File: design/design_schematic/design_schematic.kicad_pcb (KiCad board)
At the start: 2 copper layers, 22 parts, among them U1 nRF52840, X1 32MHz

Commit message: pcb place switches, leds, diodes and stabiliser right side
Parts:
- added C10: 4.7uF, ScottoKeebs_Components:Capacitor_0402, F.Cu at (553.7, 104.6)
- added C13: 4.7uF, ScottoKeebs_Components:Capacitor_0402, F.Cu at (553.7, 110.5)
- added C17: 4.7uF, ScottoKeebs_Components:Capacitor_0402, F.Cu at (553.7, 114.5)
- added C18: 1uF, ScottoKeebs_Components:Capacitor_0402, F.Cu at (553.7, 116.5)
- added C22: 470nF, ScottoKeebs_Components:Capacitor_0402, F.Cu at (553.7, 118.4)
- added C23: 4.7uF, ScottoKeebs_Components:Capacitor_0402, F.Cu at (556.5, 104.6)
- added C24: 100nF, ScottoKeebs_Components:Capacitor_0402, F.Cu at (556.5, 106.6)
- added C25: 10uF, ScottoKeebs_Components:Capacitor_0402, F.Cu at (556.5, 108.6)
- added C26: 10uF, ScottoKeebs_Components:Capacitor_0402, F.Cu at (556.5, 110.5)
- added C27: 10uF, ScottoKeebs_Components:Capacitor_0402, F.Cu at (556.5, 112.5)
- added C28: 100nF, ScottoKeebs_Components:Capacitor_0402, F.Cu at (556.5, 114.5)
- added C31: 100nF, ScottoKeebs_Components:Capacitor_0402, F.Cu at (556.5, 116.5)
- added C34: 100nF, ScottoKeebs_Components:Capacitor_0402, F.Cu at (556.5, 118.4)
- added C37: 100nF, ScottoKeebs_Components:Capacitor_0402, F.Cu at (559.4, 104.6)
- added C40: 100nF, ScottoKeebs_Components:Capacitor_0402, F.Cu at (559.4, 106.6)
- added C43: 100nF, ScottoKeebs_Components:Capacitor_0402, F.Cu at (559.4, 108.6)
- added C46: 10uF, ScottoKeebs_Components:Capacitor_0402, F.Cu at (559.4, 110.5)
- added C49: 100nF, ScottoKeebs_Components:Capacitor_0402, F.Cu at (559.4, 112.5)
- added C9: 4.7uF, ScottoKeebs_Components:Capacitor_0402, F.Cu at (550.8, 118.4)
- added D1: LED_SK6812MINI, ScottoKeebs_Components:LED_SK6812MINI, B.Cu at (74.4, 47.2)
- added D10: LED_SK6812MINI, ScottoKeebs_Components:LED_SK6812MINI, B.Cu at (131.5, 66.2)
- added D11: LED_SK6812MINI, ScottoKeebs_Components:LED_SK6812MINI, B.Cu at (150.6, 66.2)
- added D12: LED_SK6812MINI, ScottoKeebs_Components:LED_SK6812MINI, B.Cu at (169.6, 66.2)
- added D13: LED_SK6812MINI, ScottoKeebs_Components:LED_SK6812MINI, B.Cu at (74.4, 85.3)
- added D14: LED_SK6812MINI, ScottoKeebs_Components:LED_SK6812MINI, B.Cu at (93.4, 85.3)
- added D15: LED_SK6812MINI, ScottoKeebs_Components:LED_SK6812MINI, B.Cu at (112.5, 85.3)
- added D16: LED_SK6812MINI, ScottoKeebs_Components:LED_SK6812MINI, B.Cu at (131.5, 85.3)
- added D17: LED_SK6812MINI, ScottoKeebs_Components:LED_SK6812MINI, B.Cu at (150.6, 85.3)
- added D18: LED_SK6812MINI, ScottoKeebs_Components:LED_SK6812MINI, B.Cu at (172.0, 85.3)
- added D19: LED_SK6812MINI, ScottoKeebs_Components:LED_SK6812MINI, B.Cu at (88.7, 104.3)
- added D2: LED_SK6812MINI, ScottoKeebs_Components:LED_SK6812MINI, B.Cu at (93.4, 47.2)
- added D20: LED_SK6812MINI, ScottoKeebs_Components:LED_SK6812MINI, B.Cu at (117.3, 104.3)
- added D21: LED_SK6812MINI, ScottoKeebs_Components:LED_SK6812MINI, B.Cu at (136.3, 104.3)
- added D22: LED_SK6812MINI, ScottoKeebs_Components:LED_SK6812MINI, B.Cu at (155.4, 104.3)
- added D23: LED_SK6812MINI, ScottoKeebs_Components:LED_SK6812MINI, B.Cu at (174.4, 104.3)
- added D24: LED_SK6812MINI, ScottoKeebs_Components:LED_SK6812MINI, B.Cu at (69.6, 123.4)
- added D3: LED_SK6812MINI, ScottoKeebs_Components:LED_SK6812MINI, B.Cu at (112.5, 47.2)
- added D4: LED_SK6812MINI, ScottoKeebs_Components:LED_SK6812MINI, B.Cu at (131.5, 47.2)
- added D5: LED_SK6812MINI, ScottoKeebs_Components:LED_SK6812MINI, B.Cu at (150.6, 47.2)
- added D6: LED_SK6812MINI, ScottoKeebs_Components:LED_SK6812MINI, B.Cu at (172.0, 47.2)
- added D7: LED_SK6812MINI, ScottoKeebs_Components:LED_SK6812MINI, B.Cu at (74.4, 66.2)
- added D8: LED_SK6812MINI, ScottoKeebs_Components:LED_SK6812MINI, B.Cu at (93.4, 66.2)
- added D9: LED_SK6812MINI, ScottoKeebs_Components:LED_SK6812MINI, B.Cu at (112.5, 66.2)
- added Di1: Diode, ScottoKeebs_Components:Diode_SOD-123, B.Cu at (82.9, 45.5)
- added Di10: Diode, ScottoKeebs_Components:Diode_SOD-123, B.Cu at (180.5, 45.5)
- added Di11: Diode, ScottoKeebs_Components:Diode_SOD-123, B.Cu at (82.9, 64.5)
- added Di12: Diode, ScottoKeebs_Components:Diode_SOD-123, B.Cu at (101.9, 64.5)
- added Di13: Diode, ScottoKeebs_Components:Diode_SOD-123, B.Cu at (140.0, 64.5)
- added Di14: Diode, ScottoKeebs_Components:Diode_SOD-123, B.Cu at (159.1, 64.5)
- added Di15: Diode, ScottoKeebs_Components:Diode_SOD-123, B.Cu at (178.1, 64.5)
- added Di16: Diode, ScottoKeebs_Components:Diode_SOD-123, B.Cu at (101.9, 83.6)
- added Di17: Diode, ScottoKeebs_Components:Diode_SOD-123, B.Cu at (121.0, 83.6)
- added Di18: Diode, ScottoKeebs_Components:Diode_SOD-123, B.Cu at (140.0, 83.6)
- added Di19: Diode, ScottoKeebs_Components:Diode_SOD-123, B.Cu at (88.7, 104.3)
- added Di2: Diode, ScottoKeebs_Components:Diode_SOD-123, B.Cu at (159.1, 45.5)
- added Di20: Diode, ScottoKeebs_Components:Diode_SOD-123, B.Cu at (97.2, 102.6)
- added Di21: Diode, ScottoKeebs_Components:Diode_SOD-123, B.Cu at (125.8, 102.6)
- added Di22: Diode, ScottoKeebs_Components:Diode_SOD-123, B.Cu at (163.9, 102.6)
- added Di23: Diode, ScottoKeebs_Components:Diode_SOD-123, B.Cu at (182.9, 102.6)
- added Di24: Diode, ScottoKeebs_Components:Diode_SOD-123, B.Cu at (78.1, 121.7)
- added Di3: Diode, ScottoKeebs_Components:Diode_SOD-123, B.Cu at (121.0, 64.5)
- added Di4: Diode, ScottoKeebs_Components:Diode_SOD-123, B.Cu at (82.9, 83.6)
- added Di5: Diode, ScottoKeebs_Components:Diode_SOD-123, B.Cu at (159.1, 83.6)
- added Di6: Diode, ScottoKeebs_Components:Diode_SOD-123, B.Cu at (144.8, 102.6)
- added Di7: Diode, ScottoKeebs_Components:Diode_SOD-123, B.Cu at (101.9, 45.5)
- added Di8: Diode, ScottoKeebs_Components:Diode_SOD-123, B.Cu at (121.0, 45.5)
- added Di9: Diode, ScottoKeebs_Components:Diode_SOD-123, B.Cu at (140.0, 45.5)
- added IC1: XC9291B33D0R-G, SamacSys_Parts:XC9290A07E0RG, F.Cu at (546.8, 146.9)
- added IC4: 74AHCT125PW,118, SamacSys_Parts:SOP65P640X110-14N, F.Cu at (540.9, 142.1)
- added J1: USB_C_Receptacle_USB2.0_16P, Connector_USB:USB_C_Receptacle_HRO_TYPE-C-31-M-12, F.Cu at (539.9, 129.5)
- added J4: OLED_128x32, ScottoKeebs_Components:OLED_128x32, F.Cu at (531.1, 124.5)
- added J5: 0781271220, SamacSys_Parts:0781271220, F.Cu at (551.4, 125.7)
- added S1: Keyswitch, ScottoKeebs_Hotswap:Hotswap_Choc_V1_1.00u, F.Cu at (74.4, 42.5)
- added S10: Keyswitch, ScottoKeebs_Hotswap:Hotswap_Choc_V1_1.00u, F.Cu at (131.5, 61.5)
- added S11: Keyswitch, ScottoKeebs_Hotswap:Hotswap_Choc_V1_1.00u, F.Cu at (150.6, 61.5)
- added S12: Keyswitch, ScottoKeebs_Hotswap:Hotswap_Choc_V1_1.00u, F.Cu at (172.0, 61.5)
- added S13: Keyswitch, ScottoKeebs_Hotswap:Hotswap_Choc_V1_1.00u, F.Cu at (74.4, 80.6)
- added S14: Keyswitch, ScottoKeebs_Hotswap:Hotswap_Choc_V1_1.00u, F.Cu at (93.4, 80.6)
- added S15: Keyswitch, ScottoKeebs_Hotswap:Hotswap_Choc_V1_1.00u, F.Cu at (112.5, 80.6)
- added S16: Keyswitch, ScottoKeebs_Hotswap:Hotswap_Choc_V1_1.00u, F.Cu at (131.5, 80.6)
- added S17: Keyswitch, ScottoKeebs_Hotswap:Hotswap_Choc_V1_1.00u, F.Cu at (150.6, 80.6)
- added S18: Keyswitch, ScottoKeebs_Hotswap:Hotswap_Choc_V1_1.00u, F.Cu at (172.0, 80.6)
- added S2: Keyswitch, ScottoKeebs_Hotswap:Hotswap_Choc_V1_1.00u, F.Cu at (93.4, 42.5)
- added S20: Keyswitch, ScottoKeebs_Hotswap:Hotswap_Choc_V1_1.00u, F.Cu at (117.3, 99.6)
- added S21: Keyswitch, ScottoKeebs_Hotswap:Hotswap_Choc_V1_1.00u, F.Cu at (136.3, 99.6)
- added S22: Keyswitch, ScottoKeebs_Hotswap:Hotswap_Choc_V1_1.00u, F.Cu at (155.4, 99.6)
- added S23: Keyswitch, ScottoKeebs_Hotswap:Hotswap_Choc_V1_1.00u, F.Cu at (174.4, 99.6)
- added S24: Keyswitch, ScottoKeebs_Hotswap:Hotswap_Choc_V1_1.00u, F.Cu at (69.6, 118.7)
- added S3: Keyswitch, ScottoKeebs_Hotswap:Hotswap_Choc_V1_1.00u, F.Cu at (112.5, 42.5)
- added S4: Keyswitch, ScottoKeebs_Hotswap:Hotswap_Choc_V1_1.00u, F.Cu at (131.5, 42.5)
- added S5: Keyswitch, ScottoKeebs_Hotswap:Hotswap_Choc_V1_1.00u, F.Cu at (150.6, 42.5)
- added S6: Keyswitch, ScottoKeebs_Hotswap:Hotswap_Choc_V1_1.00u, F.Cu at (172.0, 42.5)
- added S7: Keyswitch, ScottoKeebs_Hotswap:Hotswap_Choc_V1_1.00u, F.Cu at (74.4, 61.5)
- added S8: Keyswitch, ScottoKeebs_Hotswap:Hotswap_Choc_V1_1.00u, F.Cu at (93.4, 61.5)
- added S9: Keyswitch, ScottoKeebs_Hotswap:Hotswap_Choc_V1_1.00u, F.Cu at (112.5, 61.5)
- added Si19: Keyswitch, ScottoKeebs_Hotswap:Hotswap_Choc_V1_1.00u, F.Cu at (88.7, 99.6)
- added St1: Stabilizer_MX_2.00u, ScottoKeebs_Stabilizer:Stabilizer_MX_2.00u, F.Cu at (69.6, 118.7)
- added St2: Stabilizer_MX_2.00u, ScottoKeebs_Stabilizer:Stabilizer_MX_2.00u, F.Cu at (88.7, 99.6)
- added U2: BQ24072RGT, Package_DFN_QFN:VQFN-16-1EP_3x3mm_P0.5mm_EP1.6x1.6mm, F.Cu at (556.4, 146.2)
- added U3: USB6B1, Package_SO:SOIC-8_3.9x4.9mm_P1.27mm, F.Cu at (549.5, 142.2)
- added U4: BQ27441-G1, Package_SON:Texas_S-PDSO-N12, F.Cu at (556.9, 141.2)
- added U5: PEC11L-4015F-S0015, SamacSys_Parts:PEC11L4015FS0015, F.Cu at (533.0, 62.1)
- added U6: PEC11L-4015F-S0015, SamacSys_Parts:PEC11L4015FS0015, F.Cu at (551.3, 62.1)
- moved L1 520.5 mm to (560.5, 144.5)
- moved L3 520.5 mm to (560.5, 146.5)
- moved L2 519.6 mm to (561.2, 139.7)
- moved L4 519.6 mm to (561.2, 141.4)
- moved X1 515.2 mm to (551.0, 133.7)
- moved C1 505.7 mm to (550.8, 104.6)
- moved C16 505.7 mm to (553.7, 112.5)
- moved C2 505.7 mm to (550.8, 106.6)
- moved C3 505.7 mm to (550.8, 108.6)
- moved C4 505.7 mm to (550.8, 110.5)
- moved C5 505.7 mm to (550.8, 112.5)
- moved C11 505.4 mm to (553.7, 106.6)
- moved C12 505.4 mm to (553.7, 108.6)
- moved C7 504.6 mm to (550.8, 114.5)
- moved C8 504.6 mm to (550.8, 116.5)
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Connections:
- net VEXT renamed 3V3
- U1 pad A10: unconnected-(U1-AIN5/P0.29-PadA10) -> /NO2
- U1 pad A12: unconnected-(U1-AIN0/P0.02-PadA12) -> /Column 0
- U1 pad A8: unconnected-(U1-AIN7/P0.31-PadA8) -> /NO
- U1 pad AA24: unconnected-(U1-SWDCLK-PadAA24) -> Net-(J6-Pin_4)
- U1 pad AC11: unconnected-(U1-P0.16-PadAC11) -> /SCL
- U1 pad AC13: unconnected-(U1-P0.18/~{RESET}-PadAC13) -> Net-(J6-Pin_1)
- U1 pad AC21: unconnected-(U1-P0.25-PadAC21) -> /2A
- U1 pad AC24: unconnected-(U1-SWDIO-PadAC24) -> Net-(J6-Pin_5)
- U1 pad AC9: unconnected-(U1-P0.14-PadAC9) -> /SDA
- U1 pad AD4: unconnected-(U1-D--PadAD4) -> D-
- U1 pad AD6: unconnected-(U1-D+-PadAD6) -> D+
- U1 pad B13: unconnected-(U1-AIN1/P0.03-PadB13) -> /Column 1
- U1 pad B15: unconnected-(U1-P1.14-PadB15) -> /CCW
- U1 pad B17: unconnected-(U1-P1.12-PadB17) -> /CW
- U1 pad G1: unconnected-(U1-P0.26-PadG1) -> /CHG
- U1 pad J1: unconnected-(U1-AIN2/P0.04-PadJ1) -> /Column 2
- U1 pad K2: unconnected-(U1-AIN3/P0.05-PadK2) -> /Column 3
- U1 pad L1: unconnected-(U1-P0.06-PadL1) -> /Column 4
- U1 pad N1: unconnected-(U1-P0.08-PadN1) -> /Column 5
- U1 pad P23: unconnected-(U1-P1.07-PadP23) -> /Row 3
- U1 pad R24: unconnected-(U1-P1.06-PadR24) -> /Row 2
- U1 pad T23: unconnected-(U1-P1.05-PadT23) -> /Row 1
- U1 pad U24: unconnected-(U1-P1.04-PadU24) -> /Row 0
- U1 pad V23: unconnected-(U1-P1.03-PadV23) -> /CCW2
- U1 pad W24: unconnected-(U1-P1.02-PadW24) -> /CW2
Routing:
- net /Row 3: track 0.00 -> 80.8 mm
- net Net-(Di24-A): track 0.00 -> 41.2 mm
- net Net-(Di20-A): track 0.00 -> 30.9 mm
- net Net-(Di6-A): track 0.00 -> 25.8 mm
- net Net-(Di5-A): track 0.00 -> 25.8 mm
- net Net-(Di4-A): track 0.00 -> 25.8 mm
- net Net-(Di23-A): track 0.00 -> 25.8 mm
- net Net-(Di22-A): track 0.00 -> 25.8 mm
- net Net-(Di21-A): track 0.00 -> 25.8 mm
- net Net-(Di19-A): track 0.00 -> 25.8 mm
- net Net-(Di18-A): track 0.00 -> 25.8 mm
- net Net-(Di17-A): track 0.00 -> 25.8 mm
- net Net-(Di16-A): track 0.00 -> 25.8 mm
- net Net-(Di9-A): track 0.00 -> 25.7 mm
- net Net-(Di8-A): track 0.00 -> 25.7 mm
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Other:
- board outline added: 282.9 x 224.2 mm

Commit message: add power planes
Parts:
- removed St2: Stabilizer_MX_2.00u, ScottoKeebs_Stabilizer:Stabilizer_MX_2.00u
- J1, U1: moved to B.Cu
- moved C1 483.3 mm to (67.8, 85.6)
- moved C10 483.3 mm to (70.7, 85.6)
- moved C11 483.3 mm to (70.7, 87.6)
- moved C12 483.3 mm to (70.7, 89.6)
- moved C13 483.3 mm to (70.7, 91.5)
- moved C16 483.3 mm to (70.7, 93.5)
- moved C17 483.3 mm to (70.7, 95.5)
- moved C18 483.3 mm to (70.7, 97.4)
- moved C2 483.3 mm to (67.8, 87.6)
- moved C22 483.3 mm to (70.7, 99.4)
- moved C23 483.3 mm to (73.6, 85.6)
- moved C24 483.3 mm to (73.6, 87.6)
- moved C25 483.3 mm to (73.6, 89.6)
- moved C26 483.3 mm to (73.6, 91.5)
- moved C27 483.3 mm to (73.6, 93.5)
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- renumbered Si19 to S19
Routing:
- net /Row 3: track 80.8 -> 7.14 mm
- net GND: track 0.00 -> 70.7 mm
- net Net-(Di24-A): track 41.2 -> 5.15 mm
- net Net-(Di21-A): track 25.8 -> 0.00 mm
- net Net-(Di6-A): track 25.8 -> 5.15 mm
- net Net-(Di5-A): track 25.8 -> 5.15 mm
- net Net-(Di4-A): track 25.8 -> 5.15 mm
- net Net-(Di23-A): track 25.8 -> 5.15 mm
- net Net-(Di22-A): track 25.8 -> 5.15 mm
- net Net-(Di19-A): track 25.8 -> 5.15 mm
- net Net-(Di18-A): track 25.8 -> 5.15 mm
- net Net-(Di17-A): track 25.8 -> 5.15 mm
- net Net-(Di16-A): track 25.8 -> 5.15 mm
- net Net-(Di9-A): track 25.7 -> 5.15 mm
- net Net-(Di8-A): track 25.7 -> 5.15 mm
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- added copper zone on In1.Cu, net 5V
- added copper zone on In2.Cu, net GND
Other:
- copper layers 2 -> 4

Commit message: vbus routing
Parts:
- removed U1: nRF52840, Package_DFN_QFN:Nordic_AQFN-73-1EP_7x7mm_P0.5mm
- added C29: 100nF, ScottoKeebs_Components:Capacitor_0603, F.Cu at (50.5, 128.6)
- added C30: 100nF, ScottoKeebs_Components:Capacitor_0603, F.Cu at (50.5, 130.6)
- added C32: 100nF, ScottoKeebs_Components:Capacitor_0603, F.Cu at (50.5, 132.6)
- added C33: 100nF, ScottoKeebs_Components:Capacitor_0603, F.Cu at (50.5, 134.5)
- added C35: 22uF, ScottoKeebs_Components:Capacitor_0603, B.Cu at (79.9, 40.0)
- added F1: 500mA, SamacSys_Parts:0603L050SLYR, B.Cu at (78.0, 36.9)
- added IC2: XC9148G50CER-G, SamacSys_Parts:XC9147_8_USP-6C, F.Cu at (204.5, 50.3)
- added IC3: nRF52833-QDAA-R7, SamacSys_Parts:QFN40P500X500X90-41N-D, B.Cu at (71.8, 112.4)
- added IC5: MCP23018T-E_SS, SamacSys_Parts:SOP65P780X200-24N, B.Cu at (71.8, 93.3)
- added J2: Battery Pos, Connector_Wire:SolderWire-2.5sqmm_1x01_D2.4mm_OD3.6mm, F.Cu at (134.0, 108.4)
- added J3: Battery Neg, Connector_Wire:SolderWire-2.5sqmm_1x01_D2.4mm_OD3.6mm, F.Cu at (134.0, 118.6)
- added L5: 1uH, Inductor_SMD:L_0603_1608Metric, F.Cu at (33.8, 59.1)
- added L6: 4.7uH, Inductor_SMD:L_0603_1608Metric, F.Cu at (33.8, 60.8)
- added R1: 5k1, Resistor_SMD:R_0603_1608Metric, B.Cu at (70.5, 42.4)
- added R10: 10k, Resistor_SMD:R_0603_1608Metric, F.Cu at (38.1, 50.8)
- added R11: 10k, Resistor_SMD:R_0603_1608Metric, F.Cu at (38.1, 53.8)
- added R12: 500, Resistor_SMD:R_0603_1608Metric, F.Cu at (38.1, 56.7)
- added R2: 5k1, Resistor_SMD:R_0603_1608Metric, B.Cu at (74.4, 42.4)
- added R3: 3k, Resistor_SMD:R_0603_1608Metric, B.Cu at (85.5, 81.1)
- added R4: 1k8, Resistor_SMD:R_0603_1608Metric, B.Cu at (82.1, 85.3)
- added R5: 10k, Resistor_SMD:R_0603_1608Metric, B.Cu at (78.6, 83.5)
- added R6: 10k, Resistor_SMD:R_0603_1608Metric, F.Cu at (33.7, 50.8)
- added R7: 10k, Resistor_SMD:R_0603_1608Metric, F.Cu at (33.7, 53.8)
- added R8: 10k, Resistor_SMD:R_0603_1608Metric, F.Cu at (33.7, 56.7)
- added R9: 10m1%, Resistor_SMD:R_0603_1608Metric, F.Cu at (38.1, 47.9)
- added S26: CL-SA-12C4-22, SamacSys_Parts:CLSA12C422, F.Cu at (204.0, 36.2)
- C1: value 12pF -> 4.7uF; footprint ScottoKeebs_Components:Capacitor_0402 -> ScottoKeebs_Components:Capacitor_0603
- C10, C13, C18, C22, C24, C25, C26, C27, C28, C31, C7, C8, C9: footprint ScottoKeebs_Components:Capacitor_0402 -> ScottoKeebs_Components:Capacitor_0603
- C11: value 100pF -> 820pF; footprint ScottoKeebs_Components:Capacitor_0402 -> ScottoKeebs_Components:Capacitor_0603
- C12: value 100nF -> 100pF; footprint ScottoKeebs_Components:Capacitor_0402 -> ScottoKeebs_Components:Capacitor_0603
- C14: value 1uF -> 12pF
- C15: value 1uF -> 1.2pF
- C16: value 47nF -> 1pF; footprint ScottoKeebs_Components:Capacitor_0402 -> ScottoKeebs_Components:Capacitor_0603
- C17, C23: footprint ScottoKeebs_Components:Capacitor_0402 -> ScottoKeebs_Components:Capacitor_0603; moved to B.Cu
- C19: value 4.7uF -> 12pF
- C2: value 12pF -> 4.7uF; footprint ScottoKeebs_Components:Capacitor_0402 -> ScottoKeebs_Components:Capacitor_0603; moved to B.Cu
- C20, C21: value 4.7uF -> 100nF
- C3: value 0.8pF -> 100nF; footprint ScottoKeebs_Components:Capacitor_0402 -> ScottoKeebs_Components:Capacitor_0603
- C34: value 100nF -> 10uF; footprint ScottoKeebs_Components:Capacitor_0402 -> ScottoKeebs_Components:Capacitor_0603
- C4: value 0.5pF -> 4.7uF; footprint ScottoKeebs_Components:Capacitor_0402 -> ScottoKeebs_Components:Capacitor_0603
- C5: value 100nF -> 1uF; footprint ScottoKeebs_Components:Capacitor_0402 -> ScottoKeebs_Components:Capacitor_0603
- C6: value 4.7uF -> 1uF
- L1: footprint Inductor_SMD:L_0402_1005Metric -> Inductor_SMD:L_0603_1608Metric
- L2: value 15nH -> 2.2nH; footprint Inductor_SMD:L_0201_0603Metric -> Inductor_SMD:L_0603_1608Metric
- U2, U3: moved to B.Cu
- moved IC1 144.2 mm to (204.2, 58.1)
- moved U3 126.8 mm to (81.4, 30.1)
- moved U2 83.9 mm to (81.6, 80.3)
- moved C18 63.7 mm to (134.1, 103.6)
- moved C23 30.0 mm to (79.0, 56.1)
- moved C1 28.4 mm to (46.2, 104.1)
- moved C10 28.4 mm to (49.1, 104.1)
- moved C11 28.4 mm to (49.1, 106.1)
- moved C12 28.4 mm to (49.1, 108.0)
- moved C13 28.4 mm to (49.1, 110.0)
- moved C16 28.4 mm to (49.1, 112.0)
- moved C3 28.4 mm to (46.2, 108.0)
- moved C37 28.4 mm to (54.9, 104.1)
- moved C4 28.4 mm to (46.2, 110.0)
- moved C40 28.4 mm to (54.9, 106.1)
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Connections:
- C1 pad 2: Net-(U1-XC1) -> 3V3
- C11 pad 1: GND -> Net-(IC3-DEC5)
- C11 pad 2: Net-(U1-DEC3) -> GND
- C12 pad 1: GND -> Net-(IC3-DEC3)
- C12 pad 2: 3V3 -> GND
- C14 pad 1: GND -> Net-(IC3-XC2)
- C14 pad 2: 3V3 -> GND
- C15 pad 1: Net-(U1-DEC4) -> Net-(C15-Pad1)
- C16 pad 1: Net-(U1-DEC4) -> GND
- C16 pad 2: GND -> Net-(IC3-ANT)
- C19 pad 1: GND -> Net-(IC3-XC1)
- C19 pad 2: /VDD_HV -> GND
- C2 pad 1: Net-(U1-XC2) -> GND
- C2 pad 2: GND -> /VBUS
- C20 pad 2: Net-(U1-DECUSB) -> 3V3
- C21 pad 1: GND -> 5V
- C21 pad 2: /VBUS -> GND
- C23 pad 2: Net-(U2-EN1) -> /VBUS
- C3 pad 1: Net-(U1-ANT) -> GND
- C3 pad 2: GND -> Net-(IC3-DEC1)
- C4 pad 2: Net-(C4-Pad2) -> Net-(IC3-DECUSB)
- C5 pad 1: GND -> 3V3
- C5 pad 2: Net-(U1-DEC1) -> GND
- C6 pad 2: 3V3 -> /DEC4
- C7 pad 1: GND -> 3V3
- C7 pad 2: 3V3 -> GND
- C8 pad 1: GND -> 3V3
- C8 pad 2: 3V3 -> GND
- D11 pad 4: Net-(D10-DOUT) -> Net-(D11-DIN)
- D12 pad 4: Net-(D11-DOUT) -> Net-(D12-DIN)
- D13 pad 4: Net-(D12-DOUT) -> Net-(D13-DIN)
- D14 pad 4: Net-(D13-DOUT) -> Net-(D10-DOUT)
- D15 pad 2: Net-(D15-DOUT) -> Net-(D11-DIN)
- D15 pad 4: Net-(D14-DOUT) -> Net-(D15-DIN)
- D16 pad 2: Net-(D16-DOUT) -> Net-(D12-DIN)
- D16 pad 4: Net-(D15-DOUT) -> Net-(D16-DIN)
- D17 pad 4: Net-(D16-DOUT) -> Net-(D13-DOUT)
- D18 pad 4: Net-(D17-DOUT) -> Net-(D14-DOUT)
- D19 pad 2: Net-(D19-DOUT) -> Net-(D15-DIN)
- D19 pad 4: Net-(D18-DOUT) -> Net-(D19-DIN)
- D2 pad 4: Net-(D1-DOUT) -> Net-(D2-DIN)
- D20 pad 2: Net-(D20-DOUT) -> Net-(D16-DIN)
- D20 pad 4: Net-(D19-DOUT) -> Net-(D20-DIN)
- D21 pad 4: Net-(D20-DOUT) -> Net-(D17-DOUT)
- D22 pad 4: Net-(D21-DOUT) -> Net-(D18-DOUT)
- D23 pad 2: Net-(D23-DOUT) -> Net-(D19-DIN)
- D23 pad 4: Net-(D22-DOUT) -> Net-(D21-DOUT)
- D24 pad 2: unconnected-(D24-DOUT-Pad2) -> Net-(D20-DIN)
- D24 pad 4: Net-(D23-DOUT) -> Net-(D22-DOUT)
- D3 pad 2: Net-(D3-DOUT) -> Net-(D2-DIN)
- D3 pad 4: Net-(D2-DOUT) -> Net-(D3-DIN)
- D4 pad 2: Net-(D4-DOUT) -> unconnected-(D4-DOUT-Pad2)
- D4 pad 4: Net-(D3-DOUT) -> Net-(D4-DIN)
- D5 pad 4: Net-(D4-DOUT) -> Net-(D1-DOUT)
- D6 pad 2: Net-(D6-DOUT) -> Net-(D10-DIN)
- D6 pad 4: Net-(D5-DOUT) -> Net-(D2-DOUT)
- D7 pad 2: Net-(D7-DOUT) -> Net-(D3-DIN)
- D7 pad 4: Net-(D6-DOUT) -> Net-(D11-DOUT)
- D8 pad 2: Net-(D8-DOUT) -> Net-(D4-DIN)
- D8 pad 4: Net-(D7-DOUT) -> Net-(D12-DOUT)
- D9 pad 2: Net-(D10-DIN) -> Net-(D13-DIN)
- D9 pad 4: Net-(D8-DOUT) -> Net-(D5-DOUT)
- L1 pad 1: Net-(C4-Pad2) -> Net-(IC3-ANT)
- L1 pad 2: Net-(U1-ANT) -> Net-(C15-Pad1)
- L2 pad 1: Net-(U1-DEC4) -> /RF
- L2 pad 2: Net-(L2-Pad2) -> Net-(C15-Pad1)
- U2 pad 13: Net-(U2-EN1) -> /VBUS
- U2 pad 6: Net-(U2-EN1) -> /VBUS
- U3 pad 1: Net-(U2-EN1) -> /VBUS
- U3 pad 8: Net-(U2-EN1) -> /VBUS
- X1 pad 1: Net-(U1-XC2) -> Net-(IC3-XC2)
- X1 pad 2: Net-(U1-XC1) -> Net-(IC3-XC1)
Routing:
- net Net-(S26-NO): track 0.00 -> 177.8 mm, vias 0 -> 2
- net Net-(J2-Pin_1): track 0.00 -> 108.2 mm, vias 0 -> 3
- net /VBUS: track 0.00 -> 86.0 mm
- net Net-(IC1-EN): track 0.00 -> 24.6 mm
- net Net-(F1-Pad1): track 0.00 -> 19.3 mm
- net Net-(J1-D--PadA7): track 0.00 -> 17.8 mm, vias 0 -> 2
- net Net-(J1-D+-PadA6): track 0.00 -> 16.6 mm, vias 0 -> 3
- net Net-(J1-CC2): track 0.00 -> 9.78 mm, vias 0 -> 2
- net Net-(J1-CC1): track 0.00 -> 8.83 mm, vias 0 -> 2
- net Net-(U2-ISET): track 0.00 -> 3.73 mm
- net Net-(U2-TS): track 0.00 -> 3.21 mm
- net Net-(U2-ILIM): track 0.00 -> 1.68 mm
- net GND: track 70.7 -> 70.9 mm, vias 0 -> 26

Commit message: prepare to change switch footprint
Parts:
- removed C37, C40, C43, C49: 100nF, ScottoKeebs_Components:Capacitor_0402
- removed C46: 10uF, ScottoKeebs_Components:Capacitor_0402
- removed IC1: XC9291B33D0R-G, SamacSys_Parts:XC9290A07E0RG
- removed L5: 1uH, Inductor_SMD:L_0603_1608Metric
- added IC6: XC9291B33D1R-G, SamacSys_Parts:XC9290A07E1RG, F.Cu at (204.5, 58.9)
- C12, C14, C15, C16, C19, C20, C22, C3, C6, L1, L2, R7, R8, R9, U4, X1: moved to B.Cu
- L3: value 10uH -> 1uH; footprint Inductor_SMD:L_0402_1005Metric -> Inductor_SMD:L_0603_1608Metric
- moved L6 170.8 mm to (204.5, 55.7), turned to 90 degrees
- moved L3 130.8 mm to (204.5, 63.2), turned to 180 degrees
- moved R9 95.1 mm to (100.5, 119.7), turned to -90 degrees
- moved R7 91.7 mm to (100.0, 117.2)
- moved R8 91.1 mm to (106.3, 111.7)
- moved C33 73.5 mm to (44.3, 61.3)
- moved L1 59.1 mm to (73.9, 115.2), turned to 180 degrees
- moved C22 58.9 mm to (107.2, 108.2), turned to 90 degrees
- moved L2 56.6 mm to (72.1, 116.8), turned to 180 degrees
- moved C29 55.7 mm to (40.3, 73.8)
- moved C30 55.2 mm to (40.3, 76.3)
- moved C34 54.6 mm to (44.3, 63.8)
- moved X1 54.0 mm to (64.8, 111.3), turned to -90 degrees
- moved C32 52.2 mm to (40.3, 81.4)
- moved C11 46.6 mm to (36.3, 61.3)
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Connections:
- L3 pad 1: Net-(L2-Pad2) -> 3V3
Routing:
- net 3V3: track 0.00 -> 198.0 mm, vias 0 -> 12
- net /NO2: track 0.00 -> 99.0 mm
- net /SDA: track 0.00 -> 89.8 mm
- net /SCL: track 0.00 -> 72.9 mm
- net /VBUS: track 86.0 -> 148.2 mm, vias 0 -> 2
- net /CHG: track 0.00 -> 60.1 mm, vias 0 -> 2
- net /DEC4: track 0.00 -> 59.5 mm
- net /NO: track 0.00 -> 52.0 mm
- net GND: track 70.9 -> 119.9 mm, vias 26 -> 52
- net Net-(J2-Pin_1): track 108.2 -> 146.1 mm, vias 3 -> 4
- net Net-(U4-V_{DD}): track 0.00 -> 21.3 mm
- net Net-(IC3-XC1): track 0.00 -> 18.4 mm
- net Net-(IC3-XC2): track 0.00 -> 18.2 mm
- net Net-(IC3-DEC3): track 0.00 -> 15.5 mm
- net Net-(U4-GPOUT): track 0.00 -> 8.50 mm, vias 0 -> 2
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- added copper zone on In1.Cu, net 3V3

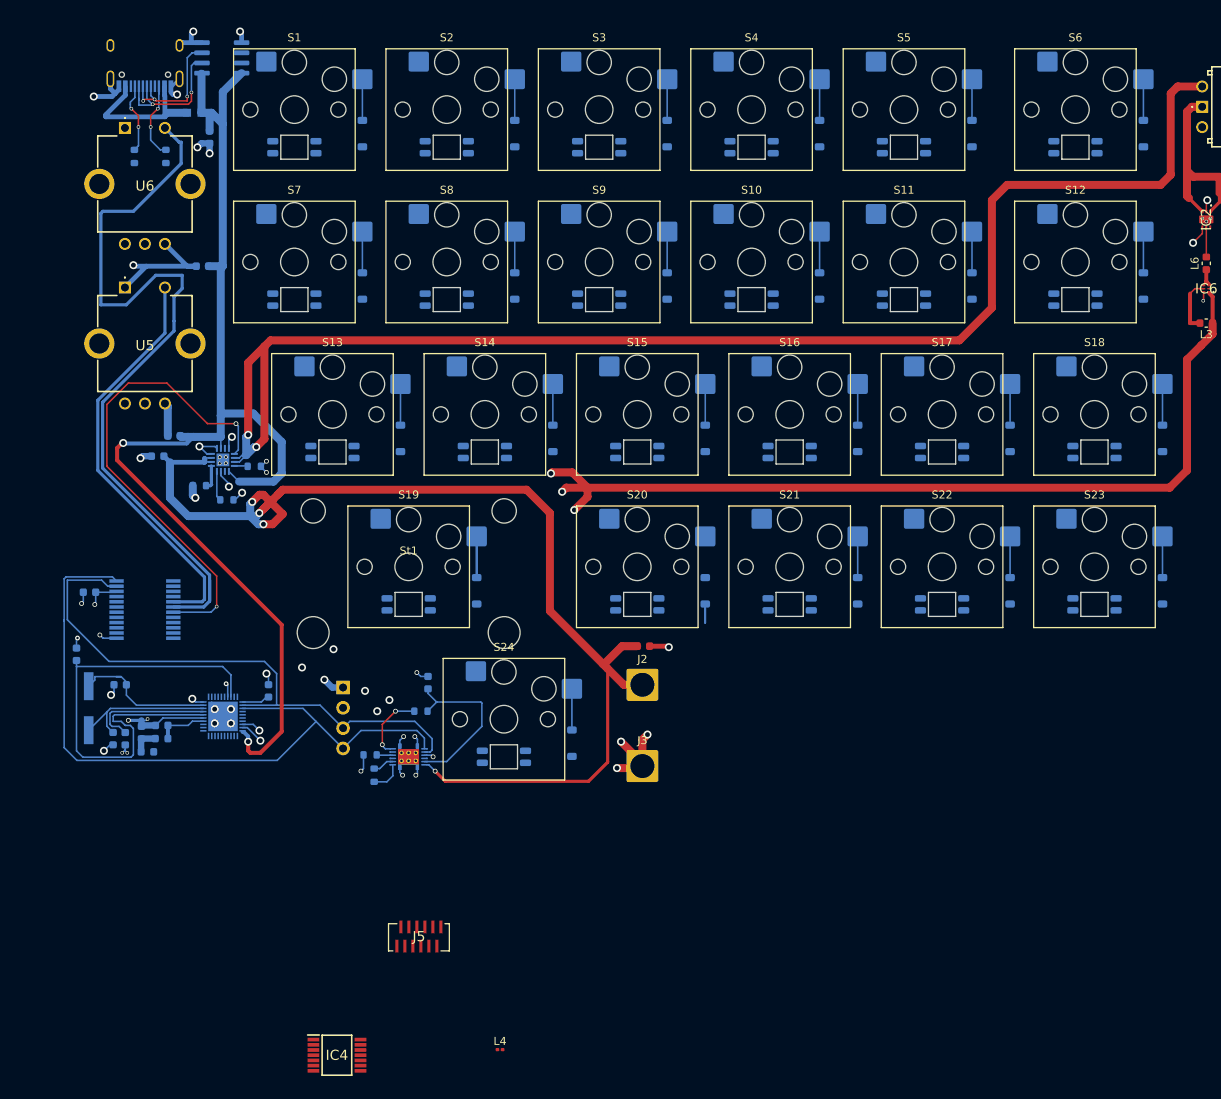
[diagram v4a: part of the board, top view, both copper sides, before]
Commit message: prepare to reroute for antenna
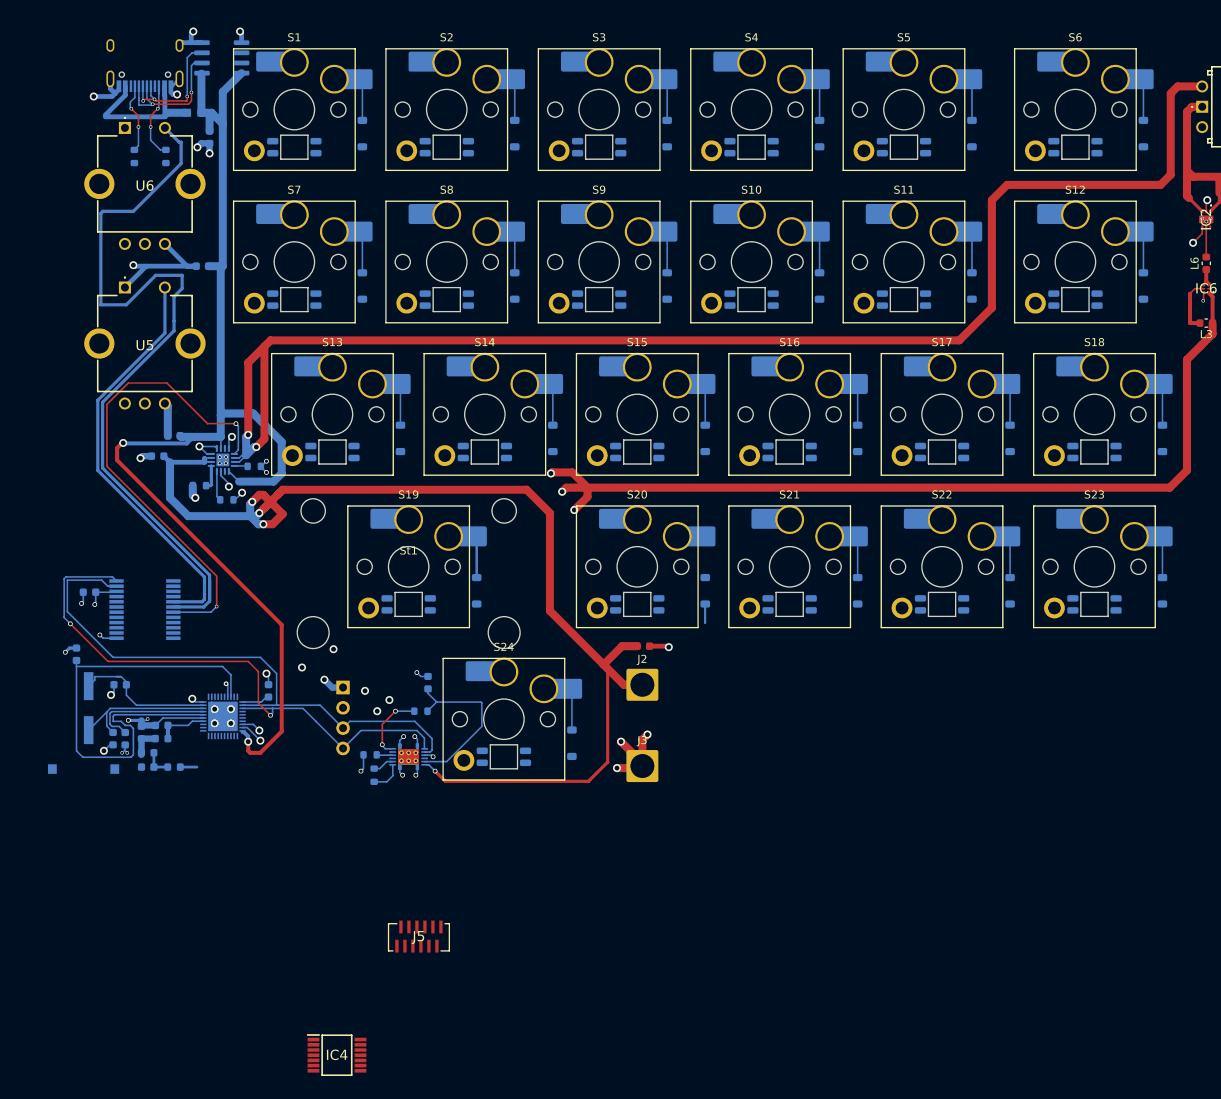
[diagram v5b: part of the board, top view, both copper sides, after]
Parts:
- added ANT1: ACAG0801-2450-T, SamacSys_Parts:ANTC8010X110N, B.Cu at (64.2, 119.0)
- added C36: 1.5pF, ScottoKeebs_Components:Capacitor_0603, B.Cu at (72.2, 118.7)
- L4: value 10uH -> 4.3nH; footprint Inductor_SMD:L_0201_0603Metric -> Inductor_SMD:L_0603_1608Metric; moved to B.Cu
- S1, S10, S11, S12, S13, S14, S15, S16, S17, S18, S19, S2, S20, S21, S22, S23, S24, S3, S4, S5, S6, S7, S8, S9: footprint ScottoKeebs_Hotswap:Hotswap_Choc_V1_1.00u -> ScottoKeebs_Hotswap:Hotswap_Choc_V1V2_Plated_1.00u
- moved L4 53.9 mm to (75.5, 118.7)
- moved L2 0.13 mm to (72.2, 116.9)
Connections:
- L4 pad 1: Net-(U1-DCCH) -> /RF
- L4 pad 2: 3V3 -> Net-(ANT1-FEED)
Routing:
- net /SDA: track 89.8 -> 73.3 mm, vias 0 -> 2
- net /RF: track 0.00 -> 3.58 mm
- net Net-(ANT1-FEED): track 0.00 -> 2.08 mm
- net /SCL: track 72.9 -> 72.3 mm
